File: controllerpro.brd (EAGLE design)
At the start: 92.7 x 33.7 mm, 10 parts

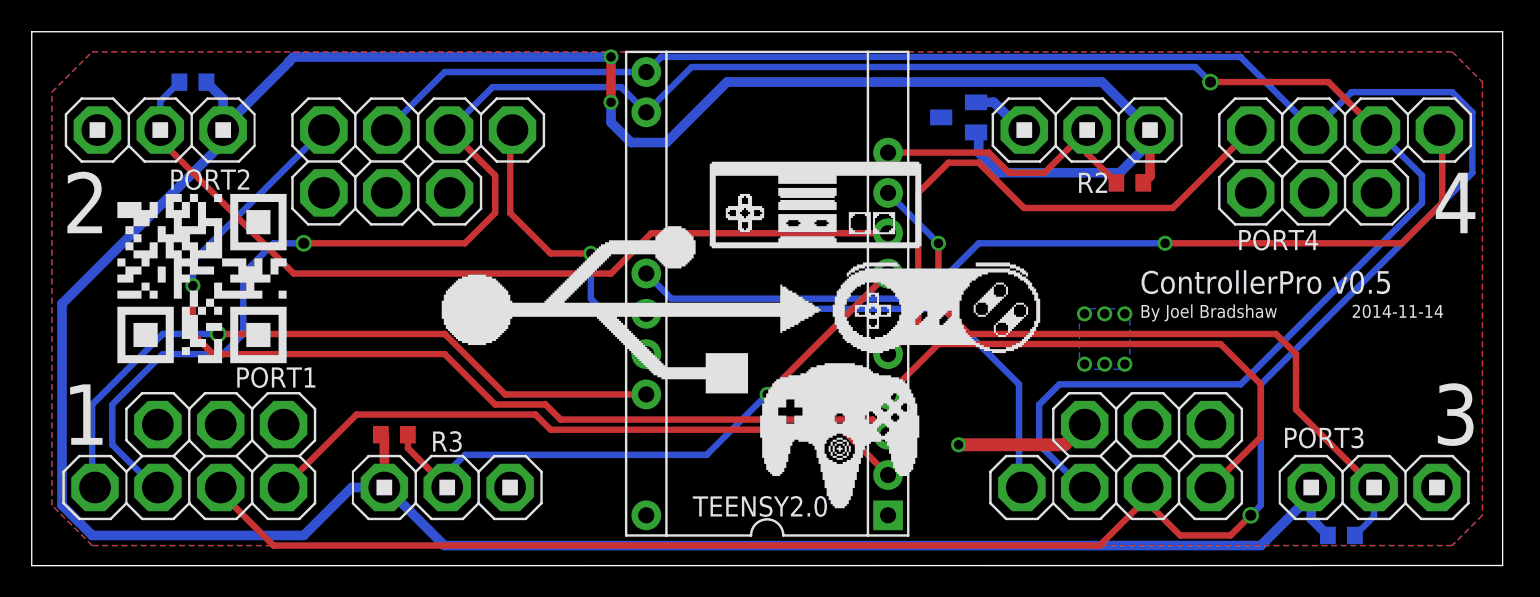
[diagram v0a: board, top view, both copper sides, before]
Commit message: Update board for Bluetooth module
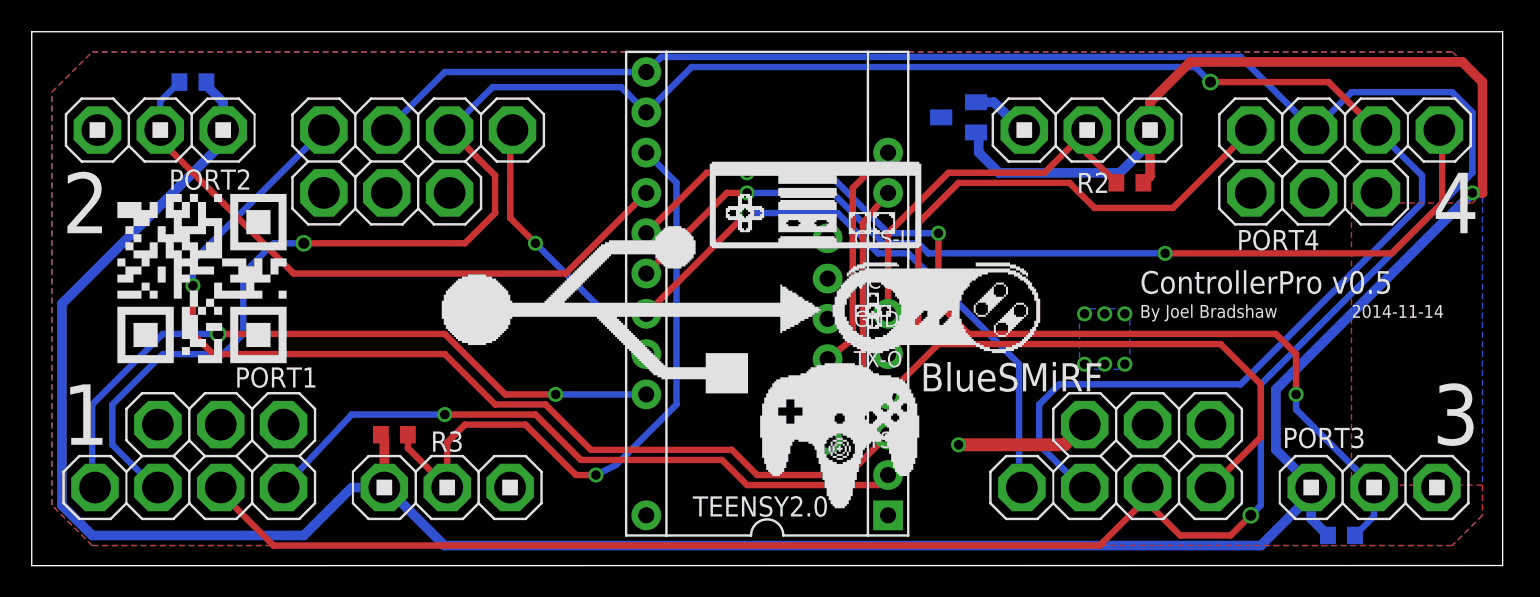
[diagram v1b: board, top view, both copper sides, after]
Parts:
- added U$1: RN42, SparkFun-Boards:RN42
- TEENSY2.0: value TEENSY_MC_PINS -> TEENSY_MC_BT_PINS; device custom:TEENSY_MC_PINS -> custom:TEENSY_MC_BT_PINS
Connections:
- new net N$2: TEENSY2.0.D2, U$1.RX-I
- new net N$5: TEENSY2.0.D3, U$1.TX-0
- net 3VDATA0: now also TEENSY2.0.B6; no longer TEENSY2.0.D2
- net 3VDATA1: now also TEENSY2.0.B7; no longer TEENSY2.0.D3
- net 3VDATA2: now also TEENSY2.0.B4; no longer TEENSY2.0.D0
- net 3VDATA3: now also TEENSY2.0.B5; no longer TEENSY2.0.D1
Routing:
- net 3VDATA0: track 46.1 -> 63.8 mm, vias 1 -> 3
- net N$5: track 0.00 -> 14.7 mm
- net N$2: track 0.00 -> 14.6 mm
- net 3VDATA3: track 54.6 -> 40.4 mm
- net V33: track 207.8 -> 196.5 mm, vias 2 -> 1
- net 3VDATA1: track 18.3 -> 24.4 mm
- net S_OR_NES0: track 32.2 -> 37.9 mm, vias 0 -> 1
- net 3VDATA2: track 38.3 -> 41.8 mm
- net 5VDATA1: track 35.9 -> 33.7 mm
- net 5VDATA3: track 62.7 -> 64.8 mm
- net S_OR_NES1: track 58.0 -> 59.8 mm, vias 1 -> 2
- net S_OR_NES3: track 19.2 -> 17.7 mm
- net 5VDATA2: track 41.6 -> 42.2 mm, vias 0 -> 1
- net S_OR_NES2: track 44.0 -> 43.7 mm, vias 1 -> 2

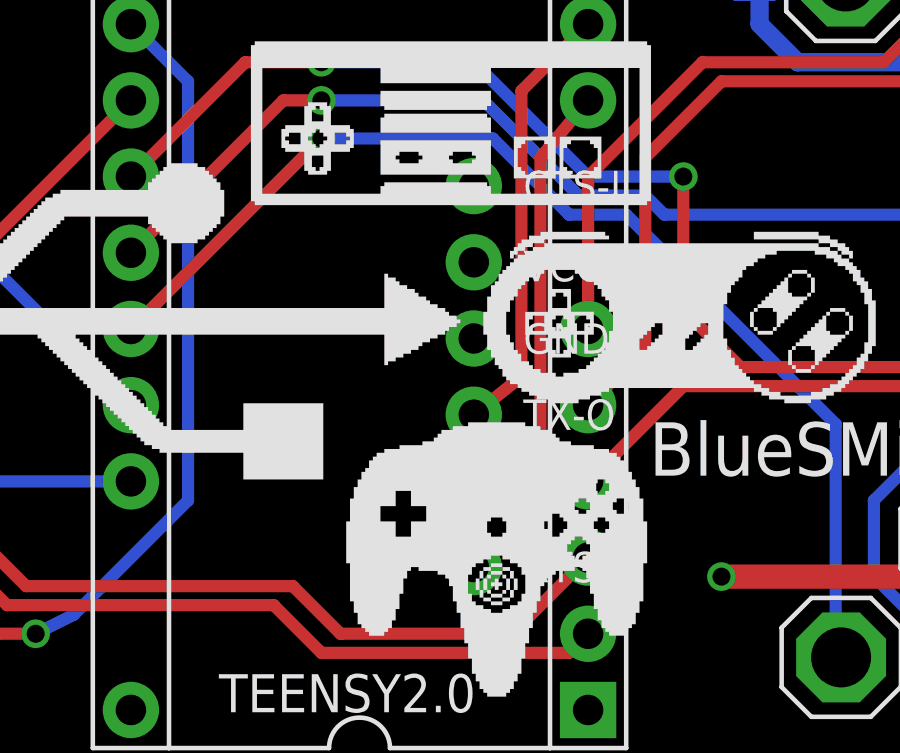
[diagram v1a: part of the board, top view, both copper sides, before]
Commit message: Connect bluetooth power, etc:
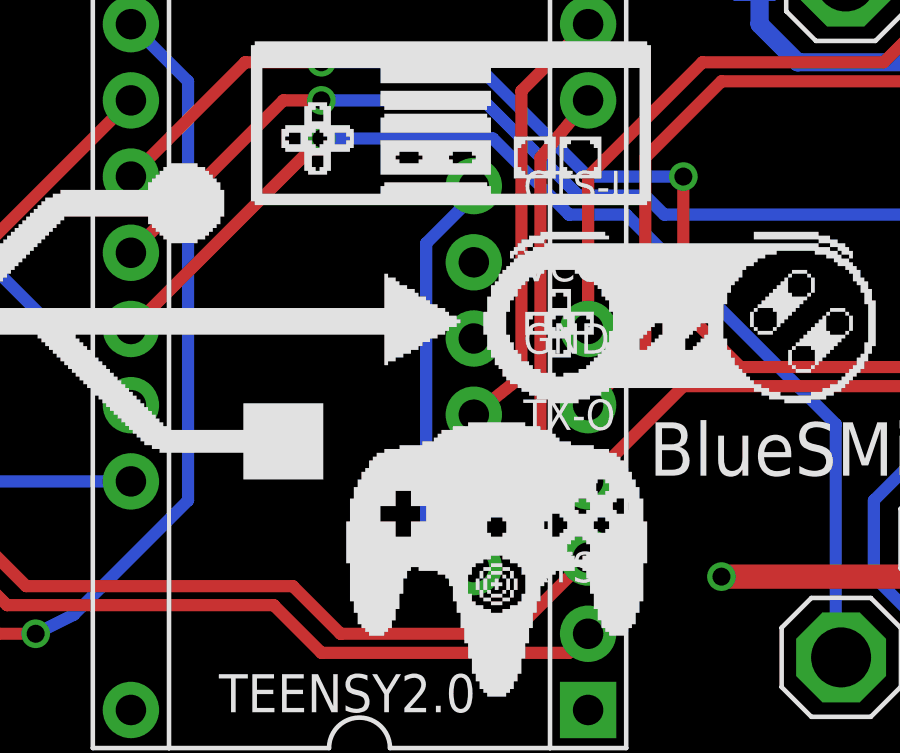
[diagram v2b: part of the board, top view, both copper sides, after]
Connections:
- new net N$6: U$1.CTS-I, U$1.RTS-0
- net GND: now also U$1.GND
- net VCC: now also U$1.VCC
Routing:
- net N$6: track 0.00 -> 14.0 mm
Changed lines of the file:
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@@
 <wire x1="65.1002" y1="7.62" x2="66.3702" y2="8.89" width="0.8128" layer="1"/>
 <via x="58.42" y="7.62" extent="1-16" drill="0.6"/>
+<contactref element="U$1" pad="VCC"/>
 </signal>
 <signal name="GND" class="1">
@@
 <vertex x="66.3575" y="16.1925"/>
 </polygon>
+<contactref element="U$1" pad="GND"/>
 </signal>
 <signal name="V33">
@@
 <wire x1="51.7525" y1="23.8125" x2="51.7525" y2="14.2875" width="0.4064" layer="1"/>
 </signal>
+<signal name="N$6">
+<contactref element="U$1" pad="CTS-I"/>
+<contactref element="U$1" pad="RTS-0"/>
+<wire x1="50.165" y1="20.6375" x2="50.165" y2="20.32" width="0.4064" layer="16"/>
+<wire x1="50.165" y1="20.32" x2="48.5775" y2="18.7325" width="0.4064" layer="16"/>
+<wire x1="48.5775" y1="18.7325" x2="48.5775" y2="9.525" width="0.4064" layer="16"/>
+<wire x1="48.5775" y1="9.525" x2="50.165" y2="7.9375" width="0.4064" layer="16"/>
+</signal>
 </signals>

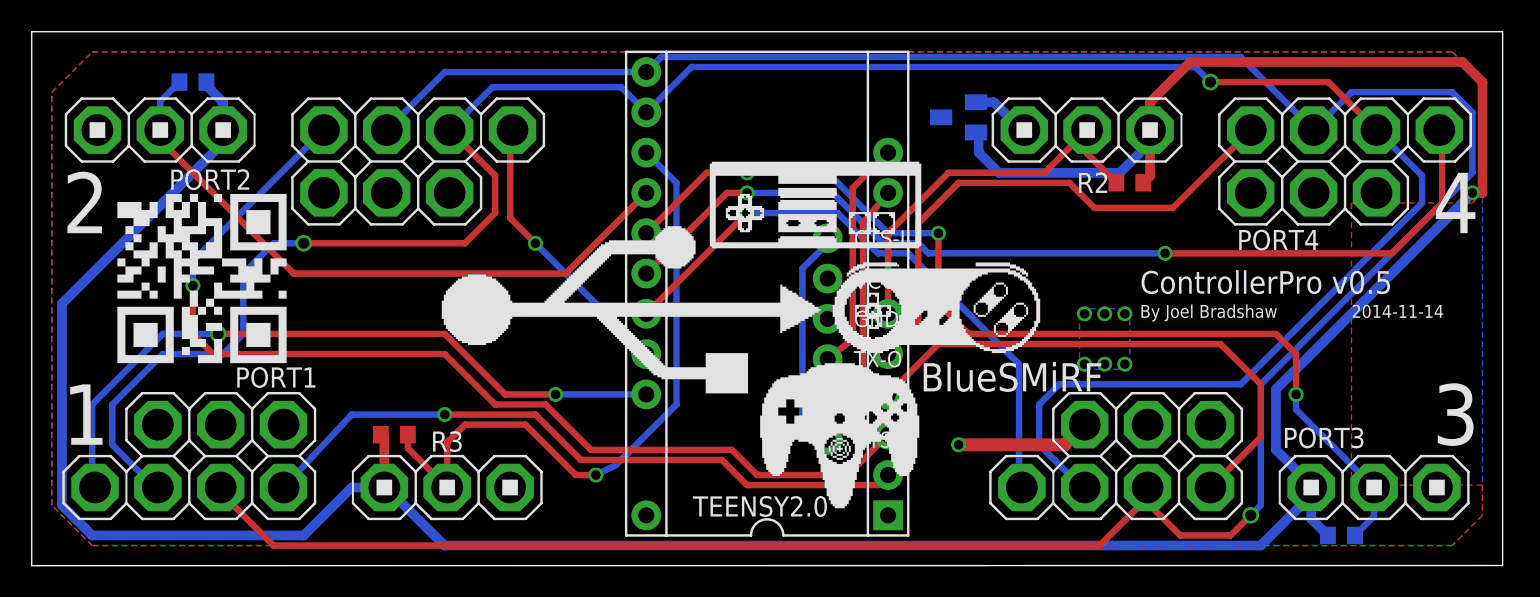
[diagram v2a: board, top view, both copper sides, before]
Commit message: Switch VCC to 3.3v
Remove VREG, supply NES/SNES and N64 all with 3.3v
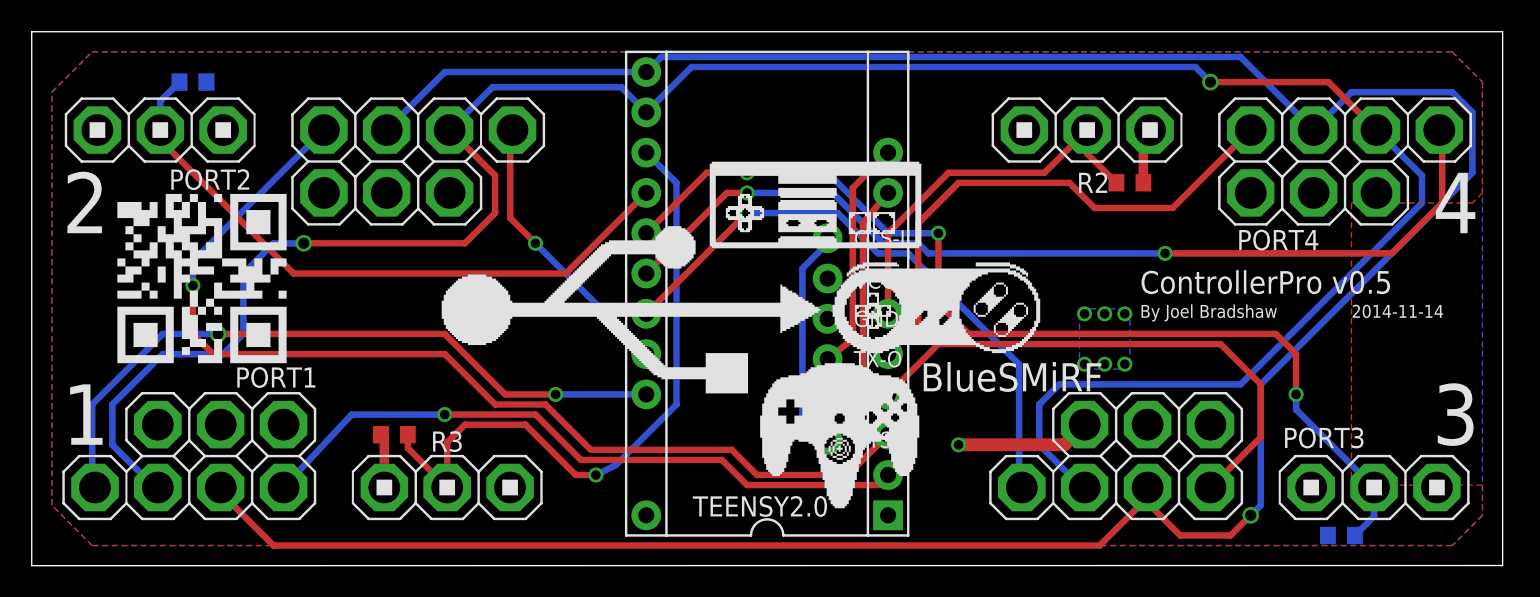
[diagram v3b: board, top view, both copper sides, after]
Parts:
- removed VREG: MCP1703CB, linear:SOT23
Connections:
- removed net V33: PORT1.5, PORT2.5, PORT3.5, PORT4.5, R1.2, R2.1, R3.2, R4.1, VREG.2
- net GND: no longer VREG.1
- net VCC: now also PORT1.5, PORT2.5, PORT3.5, PORT4.5, R1.2, R2.1, R3.2, R4.1; no longer VREG.3
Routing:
- net V33: track 196.5 -> 0.00 mm, vias 1 -> 0
- net VCC: track 8.48 -> 15.4 mm
- net GND: track 3.77 -> 0.17 mm
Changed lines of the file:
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@@
 <attribute name="VALUE" x="32.2834" y="31.4198" size="1.27" layer="27" rot="R180"/>
-</element>
-<element name="VREG" library="linear" package="SOT23" value="MCP1703CB" x="58.42" y="28.2575" smashed="yes" rot="MR270">
-<attribute name="NAME" x="51.1175" y="29.464" size="1.27" layer="26" rot="MR180"/>
-<attribute name="VALUE" x="61.595" y="30.1625" size="1.27" layer="28" rot="MR270"/>
 </element>
 <element name="TEENSY2.0" library="custom" package="TEENSY_MC_BT_PINS" value="TEENSY_MC_BT_PINS" x="46.355" y="17.145" smashed="yes" rot="R90">
@@
 <contactref element="PORT1" pad="10"/>
 <contactref element="PORT4" pad="10"/>
-<contactref element="VREG" pad="3"/>
 <contactref element="TEENSY2.0" pad="+5V"/>
 <polygon width="0.6096" layer="16" isolate="0.4064" rank="2">
@@
 <via x="58.42" y="7.62" extent="1-16" drill="0.6"/>
 <contactref element="U$1" pad="VCC"/>
+<contactref element="R2" pad="1"/>
+<contactref element="PORT3" pad="5"/>
+<contactref element="R1" pad="2"/>
+<contactref element="PORT4" pad="5"/>
+<contactref element="R3" pad="2"/>
+<contactref element="PORT1" pad="5"/>
+<contactref element="R4" pad="1"/>
+<contactref element="PORT2" pad="5"/>
+<wire x1="22.225" y1="4.9276" x2="22.225" y2="8.04" width="0.6096" layer="1"/>
+<wire x1="22.225" y1="8.04" x2="22.01" y2="8.255" width="0.6096" layer="1"/>
+<wire x1="70.065" y1="24.13" x2="70.065" y2="27.0374" width="0.6096" layer="1"/>
+<wire x1="70.065" y1="27.0374" x2="70.485" y2="27.4574" width="0.6096" layer="1"/>
 </signal>
 <signal name="GND" class="1">
@@
 <contactref element="PORT2" pad="7"/>
 <contactref element="PORT3" pad="7"/>
-<contactref element="VREG" pad="1"/>
 <contactref element="PORT1" pad="7"/>
 <polygon width="0.6096" layer="1" isolate="0.4064">
@@
 </polygon>
 <contactref element="TEENSY2.0" pad="GND"/>
-<wire x1="60.6425" y1="29.21" x2="62.3951" y2="27.4574" width="0.6096" layer="16"/>
 <wire x1="62.3951" y1="27.4574" x2="62.5602" y2="27.4574" width="0.6096" layer="16"/>
-<wire x1="59.52" y1="29.2075" x2="59.5225" y2="29.21" width="0.6096" layer="16"/>
-<wire x1="59.5225" y1="29.21" x2="60.6425" y2="29.21" width="0.6096" layer="16"/>
 <via x="67.6275" y="15.875" extent="1-16" drill="0.6"/>
 <via x="66.3575" y="15.875" extent="1-16" drill="0.6"/>
@@
 <contactref element="U$1" pad="GND"/>
 </signal>
-<signal name="V33">
-<contactref element="PORT4" pad="5"/>
-<contactref element="PORT3" pad="5"/>
-<contactref element="PORT1" pad="5"/>
-<contactref element="PORT2" pad="5"/>
-<contactref element="VREG" pad="2"/>
-<wire x1="77.47" y1="1.27" x2="26.0096" y2="1.27" width="0.6096" layer="16"/>
-<wire x1="77.47" y1="1.27" x2="80.645" y2="4.445" width="0.6096" layer="16"/>
-<wire x1="80.645" y1="4.445" x2="80.645" y2="4.9276" width="0.6096" layer="16"/>
-<wire x1="68.58" y1="24.765" x2="70.485" y2="26.67" width="0.6096" layer="16"/>
-<wire x1="70.485" y1="26.67" x2="70.485" y2="27.4574" width="0.6096" layer="16"/>
-<wire x1="22.225" y1="4.9276" x2="20.1676" y2="4.9276" width="0.6096" layer="16"/>
-<wire x1="20.1676" y1="4.9276" x2="17.145" y2="1.905" width="0.6096" layer="16"/>
-<wire x1="17.145" y1="1.905" x2="3.81" y2="1.905" width="0.6096" layer="16"/>
-<wire x1="3.81" y1="1.905" x2="1.905" y2="3.81" width="0.6096" layer="16"/>
-<wire x1="1.905" y1="3.81" x2="1.905" y2="16.51" width="0.6096" layer="16"/>
-<wire x1="1.905" y1="16.51" x2="12.065" y2="26.67" width="0.6096" layer="16"/>
-<wire x1="12.065" y1="26.67" x2="12.065" y2="27.4574" width="0.6096" layer="16"/>
-<wire x1="22.225" y1="4.9276" x2="22.352" y2="4.9276" width="0.6096" layer="16"/>
-<wire x1="22.352" y1="4.9276" x2="26.0096" y2="1.27" width="0.6096" layer="16"/>
-<contactref element="R1" pad="2"/>
-<contactref element="R2" pad="1"/>
-<contactref element="R4" pad="1"/>
-<contactref element="R3" pad="2"/>
-<wire x1="22.01" y1="8.255" x2="22.225" y2="8.04" width="0.6096" layer="1"/>
-<wire x1="22.225" y1="8.04" x2="22.225" y2="4.9276" width="0.6096" layer="1"/>
-<wire x1="81.7" y1="1.905" x2="80.645" y2="2.96" width="0.6096" layer="16"/>
-<wire x1="80.645" y1="2.96" x2="80.645" y2="4.9276" width="0.6096" layer="16"/>
-<wire x1="70.065" y1="24.13" x2="70.485" y2="24.55" width="0.6096" layer="1"/>
-<wire x1="70.485" y1="24.55" x2="70.485" y2="27.4574" width="0.6096" layer="1"/>
-<wire x1="68.58" y1="24.765" x2="60.96" y2="24.765" width="0.6096" layer="16"/>
-<wire x1="59.52" y1="27.3075" x2="59.69" y2="27.1375" width="0.6096" layer="16"/>
-<wire x1="59.69" y1="27.1375" x2="59.69" y2="26.035" width="0.6096" layer="16"/>
-<wire x1="59.69" y1="26.035" x2="60.96" y2="24.765" width="0.6096" layer="16"/>
-<wire x1="12.065" y1="27.4574" x2="12.065" y2="29.21" width="0.6096" layer="16"/>
-<wire x1="12.065" y1="29.21" x2="11.01" y2="30.265" width="0.6096" layer="16"/>
-<wire x1="11.01" y1="30.265" x2="11.01" y2="30.48" width="0.6096" layer="16"/>
-<wire x1="80.645" y1="4.9276" x2="80.645" y2="5.08" width="0.6096" layer="16"/>
-<wire x1="80.645" y1="5.08" x2="78.4225" y2="7.3025" width="0.6096" layer="16"/>
-<wire x1="78.4225" y1="7.3025" x2="78.4225" y2="11.1125" width="0.6096" layer="16"/>
-<wire x1="78.4225" y1="11.1125" x2="90.805" y2="23.495" width="0.6096" layer="16"/>
-<via x="90.805" y="23.495" extent="1-16" drill="0.6"/>
-<wire x1="90.805" y1="23.495" x2="91.44" y2="23.495" width="0.6096" layer="1"/>
-<wire x1="91.44" y1="23.495" x2="91.44" y2="30.48" width="0.6096" layer="1"/>
-<wire x1="91.44" y1="30.48" x2="90.17" y2="31.75" width="0.6096" layer="1"/>
-<wire x1="90.17" y1="31.75" x2="73.025" y2="31.75" width="0.6096" layer="1"/>
-<wire x1="73.025" y1="31.75" x2="70.485" y2="29.21" width="0.6096" layer="1"/>
-<wire x1="70.485" y1="29.21" x2="70.485" y2="27.4574" width="0.6096" layer="1"/>
-</signal>
 <signal name="5VDATA0">
